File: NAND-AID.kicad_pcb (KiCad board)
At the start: 2 copper layers, 33.7 x 21.4 mm, 21 parts

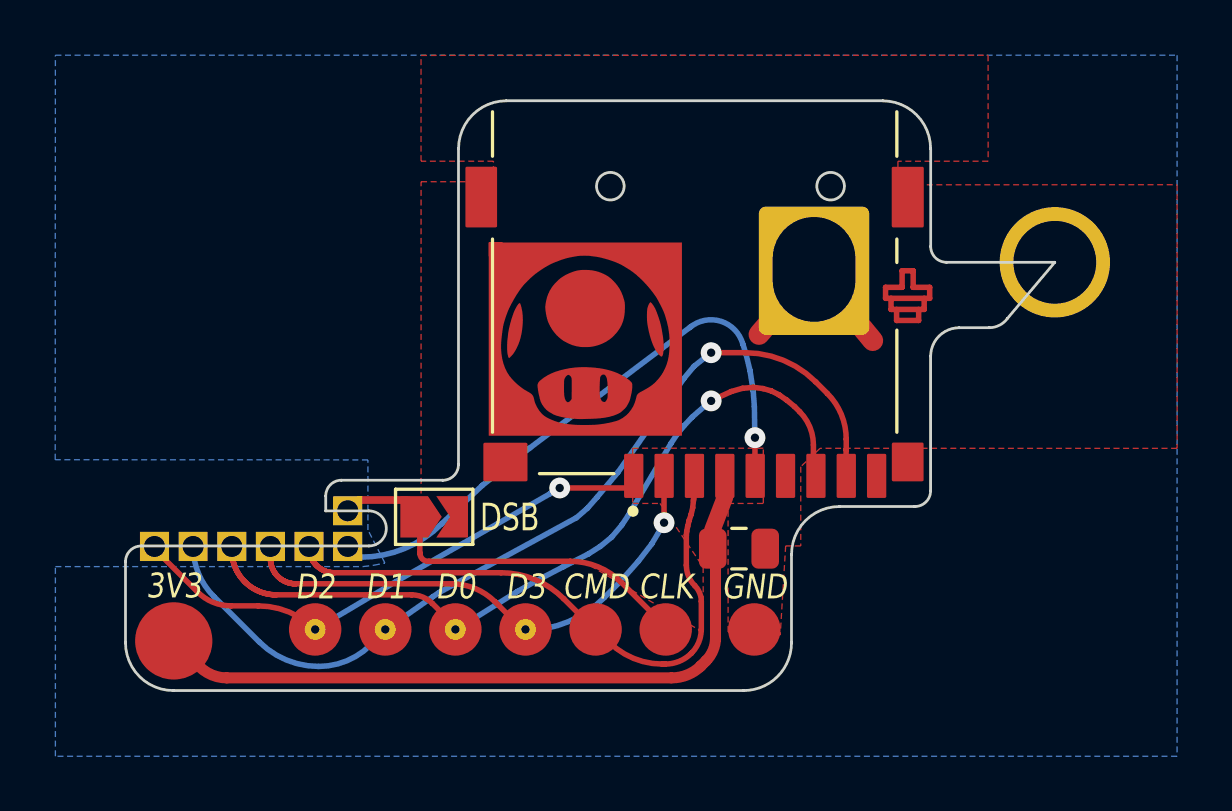
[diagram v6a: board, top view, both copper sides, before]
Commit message: Change GND hole
Signed-off-by: Thomas Rohloff <v10lator@myway.de>
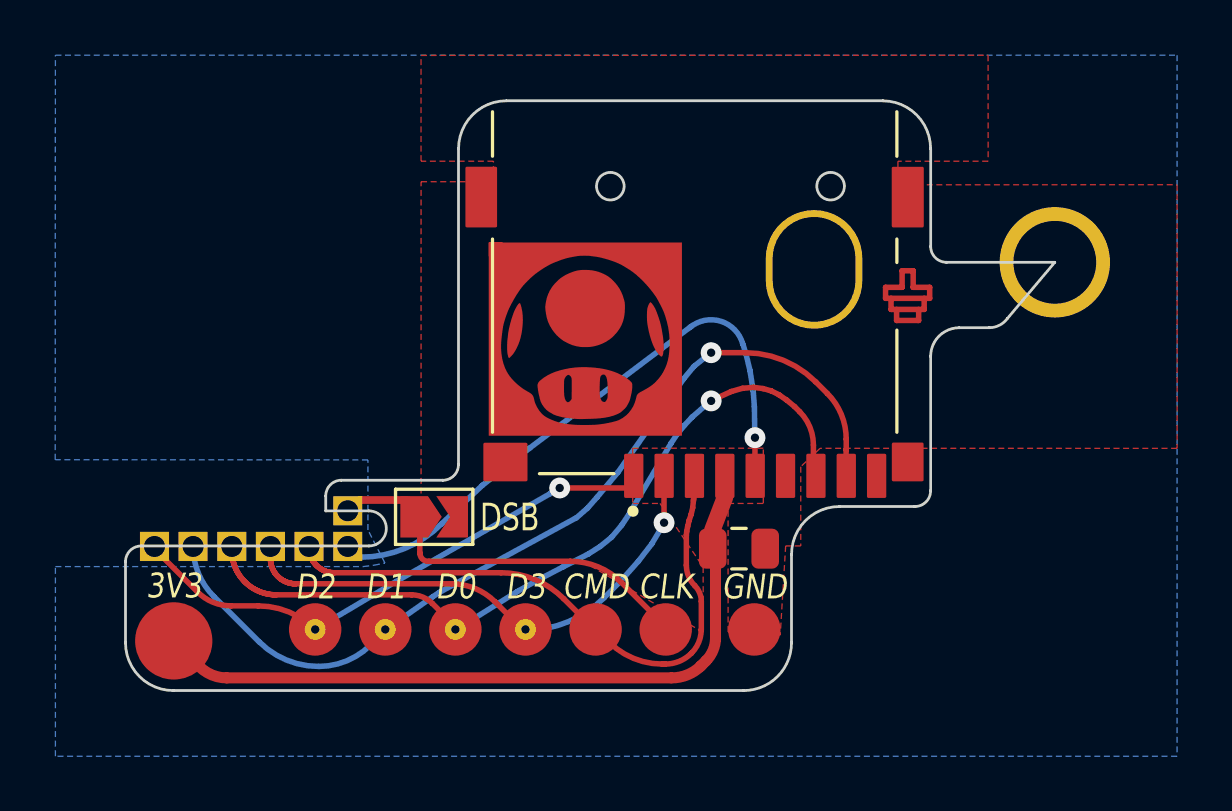
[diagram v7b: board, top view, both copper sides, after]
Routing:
- net GND: track 15.2 -> 8.80 mm
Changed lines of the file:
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@@
         (effects (font (size 1 1) (thickness 0.15)))
     )
-    (pad "" thru_hole roundrect (at 0 0) (size 4 4.65) (drill oval 3 3.8 (offset 0 0.05)) (property pad_prop_castellated) (layers "*.Cu" "*.Mask") (roundrect_rratio 0.0625)
-      (net 2 "GND") (solder_mask_margin 0.0001) (zone_connect 1) (thermal_bridge_width 0.755) (thermal_gap 0.15))
+    (pad "" thru_hole oval (at 0 0) (size 3.5 4.3) (drill oval 3 3.8) (property pad_prop_castellated) (layers "*.Cu" "*.Mask")
+      (net 2 "GND") (zone_connect 1) (thermal_bridge_width 0.4) (thermal_bridge_angle 45) (thermal_gap 0.3))
   )
   (gr_poly
@@
   (segment (start 158.077221 97.309854) (end 158.077382 96.7101) (width 0.2) (layer "F.Cu") (net 2))
   (segment (start 157.077 97.7088) (end 158.676 97.708832) (width 0.2) (layer "F.Cu") (net 2))
-  (segment (start 154.487 96.66) (end 156.613639 99.240934) (width 0.755) (layer "F.Cu") (net 2))
   (segment (start 157.676958 97.309854) (end 157.677122 96.7101) (width 0.2) (layer "F.Cu") (net 2))
   (segment (start 158.676474 97.3099) (end 158.676474 97.7088) (width 0.2) (layer "F.Cu") (net 2))
-  (segment (start 154.487 96.66) (end 152.492049 99.017263) (width 0.755) (layer "F.Cu") (net 2))
   (segment (start 158.077221 97.309854) (end 158.676 97.3099) (width 0.2) (layer "F.Cu") (net 2))
   (segment (start 157.076854 97.3099) (end 157.076854 97.7088) (width 0.2) (layer "F.Cu") (net 2))
@@
       )
     )
+  )
+  (zone (net 0) (net_name "") (layer "B.Cu") (hatch edge 0.5)
+    (connect_pads (clearance 0))
+    (min_thickness 0.25) (filled_areas_thickness no)
+    (keepout (tracks allowed) (vias allowed) (pads allowed) (copperpour not_allowed) (footprints allowed))
+    (fill (thermal_gap 0.5) (thermal_bridge_width 0.5))
+    (polygon
+      (pts
+        (xy 152.737373 95.193457)
+        (xy 152.855358 95.006538)
+        (xy 152.978264 94.868893)
+        (xy 155.993965 94.868831)
+        (xy 156.146788 95.037653)
+        (xy 156.225431 95.16904)
+        (xy 154.470706 98.405381)
+      )
+    )
